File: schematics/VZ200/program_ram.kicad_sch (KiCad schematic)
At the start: 4 parts, among them U101 74LS138, U102 6116, U103 6116, U104 6116

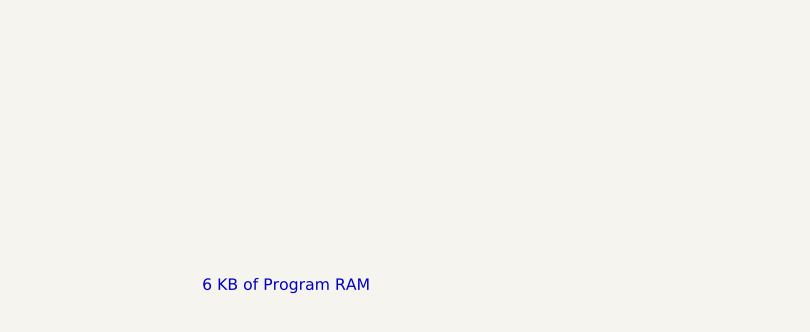
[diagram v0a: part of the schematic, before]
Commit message: Schematic for the VZ200 printer interface
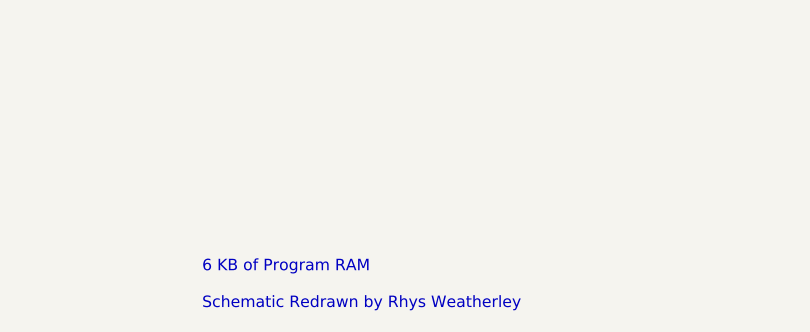
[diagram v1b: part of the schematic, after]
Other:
- note added: "6 KB of Program RAM Schematic Redrawn by Rhys Weatherley"
- note removed: "6 KB of Program RAM"
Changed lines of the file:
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@@
     (effects (font (size 1.27 1.27)) (justify left bottom))
   )
-  (text "6 KB of Program RAM" (at 184.785 174.625 0)
+  (text "6 KB of Program RAM\n\nSchematic Redrawn by Rhys Weatherley"
+    (at 184.785 176.53 0)
     (effects (font (size 1.27 1.27)) (justify left bottom))
   )

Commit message: Mention that the 6K of Program RAM is on a separate PCB
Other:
- note added: "Program RAM Schematic Redrawn by Rhys Weatherley"
- note added: "The original schematic listed these chips as U1' - U4' They have been renumbered to U101 - U104 here. The 6K of Program RAM is on a separate PCB for the VZ200. The Laser 210 only had 2K of Program RAM, which corresponds to U102 in this schematic. U101, U103, and U104 are not present on the Laser 210."
- note removed: "6 KB of Program RAM Schematic Redrawn by Rhys Weatherley"
- note removed: "The original schematic listed these chips as U1' - U4' They have been renumbered to U101 - U104 here."
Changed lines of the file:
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@@
     (stroke (width 0) (type default))
   )
-  (text "The original schematic listed these chips as U1' - U4'\nThey have been renumbered to U101 - U104 here."
-    (at 142.875 135.255 0)
+  (text "The original schematic listed these chips as U1' - U4'\nThey have been renumbered to U101 - U104 here.  The 6K of\nProgram RAM is on a separate PCB for the VZ200.\n\nThe Laser 210 only had 2K of Program RAM, which corresponds\nto U102 in this schematic.  U101, U103, and U104 are not\npresent on the Laser 210."
+    (at 135.89 144.78 0)
     (effects (font (size 1.27 1.27)) (justify left bottom))
   )
@@
     (effects (font (size 1.27 1.27)) (justify left bottom))
   )
-  (text "6 KB of Program RAM\n\nSchematic Redrawn by Rhys Weatherley"
-    (at 184.785 176.53 0)
+  (text "Program RAM\n\nSchematic Redrawn by Rhys Weatherley" (at 184.785 176.53 0)
     (effects (font (size 1.27 1.27)) (justify left bottom))
   )

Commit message: Add title and revision details to the schematic sheets
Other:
- title: (none) -> VZ200 Computer
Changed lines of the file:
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@@
 (kicad_sch (version 20230121) (generator eeschema)
   (paper "A4")
+  (title_block
+    (title "VZ200 Computer")
+    (date "2024-01-01")
+    (rev "1")
+  )
   (junction (at 130.175 44.45) (diameter 0) (color 0 0 0 0)
   )

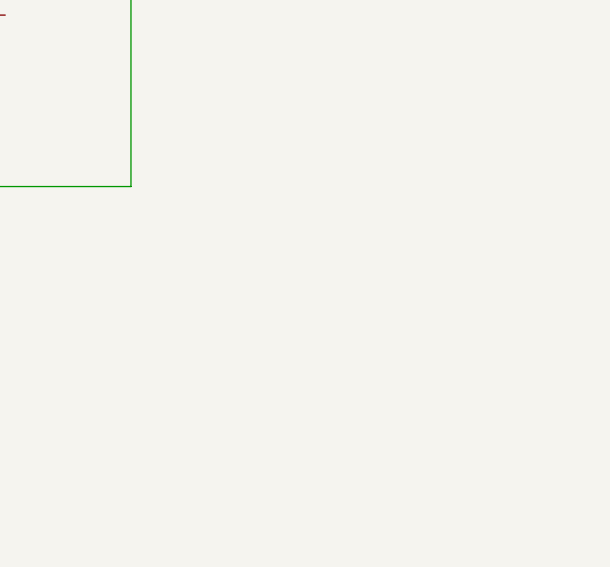
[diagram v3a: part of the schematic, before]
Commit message: Update motherboard schematic based on inspection of the actual board
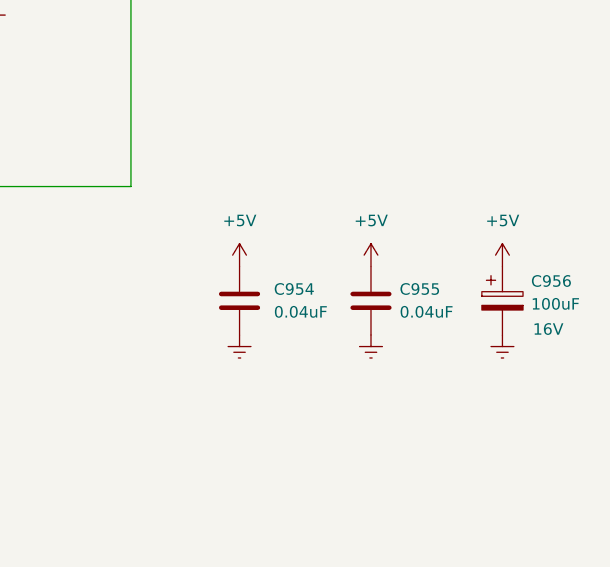
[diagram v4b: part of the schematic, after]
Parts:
- added C954, C955: 0.04uF, symbol Device:C
- added C956: 100uF, symbol Device:C_Polarized
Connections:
- net +5V: now also C954.1, C955.1, C956.1
- net Earth: now also C954.2, C955.2, C956.2
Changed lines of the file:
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@@
   (title_block
     (title "VZ200 Computer")
-    (date "2024-01-01")
-    (rev "1")
+    (date "2024-01-05")
+    (rev "2")
   )
   (junction (at 130.175 44.45) (diameter 0) (color 0 0 0 0)
@@
     (property "Intersheetrefs" "${INTERSHEET_REFS}" (at 223.3302 96.52 0)
       (effects (font (size 1.27 1.27)) (justify left) hide)
+    )
+  )
+  (symbol (lib_id "power:+5V") (at 245.745 133.35 0) (unit 1)
+    (in_bom yes) (on_board yes) (dnp no) (fields_autoplaced)
+    (property "Reference" "#PWR0149" (at 245.745 137.16 0)
+      (effects (font (size 1.27 1.27)) hide)
+    )
+    (property "Value" "+5V" (at 245.745 128.27 0)
+      (effects (font (size 1.27 1.27)))
+    )
+    (property "Footprint" "" (at 245.745 133.35 0)
+      (effects (font (size 1.27 1.27)) hide)
+    )
+    (property "Datasheet" "" (at 245.745 133.35 0)
+      (effects (font (size 1.27 1.27)) hide)
+    )
+    (pin "1")
+    (instances
+      (project "VZ200"
+        (path "/5e5f5998-714c-4695-b6b0-5b20d6c62fd6/0f5ef76c-8fbc-47f1-bc85-d4b3dcf632f6"
+          (reference "#PWR0149") (unit 1)
+        )
+      )
+    )
+  )
+  (symbol (lib_id "power:+5V") (at 260.35 133.35 0) (unit 1)
+    (in_bom yes) (on_board yes) (dnp no) (fields_autoplaced)
+    (property "Reference" "#PWR0151" (at 260.35 137.16 0)
+      (effects (font (size 1.27 1.27)) hide)
+    )
+    (property "Value" "+5V" (at 260.35 128.27 0)
+      (effects (font (size 1.27 1.27)))
+    )
+    (property "Footprint" "" (at 260.35 133.35 0)
+      (effects (font (size 1.27 1.27)) hide)
+    )
+    (property "Datasheet" "" (at 260.35 133.35 0)
+      (effects (font (size 1.27 1.27)) hide)
+    )
+    (pin "1")
+    (instances
+      (project "VZ200"
+        (path "/5e5f5998-714c-4695-b6b0-5b20d6c62fd6/0f5ef76c-8fbc-47f1-bc85-d4b3dcf632f6"
+          (reference "#PWR0151") (unit 1)
+        )
+      )
+    )
+  )
+  (symbol (lib_id "power:Earth") (at 245.745 140.97 0) (unit 1)
+    (in_bom yes) (on_board yes) (dnp no) (fields_autoplaced)
+    (property "Reference" "#PWR0150" (at 245.745 147.32 0)
+      (effects (font (size 1.27 1.27)) hide)
+    )
+    (property "Value" "Earth" (at 245.745 144.78 0)
+      (effects (font (size 1.27 1.27)) hide)
+    )
+    (property "Footprint" "" (at 245.745 140.97 0)
+      (effects (font (size 1.27 1.27)) hide)
+    )
+    (property "Datasheet" "~" (at 245.745 140.97 0)
+      (effects (font (size 1.27 1.27)) hide)
+    )
+    (pin "1")
+    (instances
+      (project "VZ200"
+        (path "/5e5f5998-714c-4695-b6b0-5b20d6c62fd6/0f5ef76c-8fbc-47f1-bc85-d4b3dcf632f6"
+          (reference "#PWR0150") (unit 1)
+        )
+      )
     )
   )
@@
     )
   )
+  (symbol (lib_id "Device:C") (at 231.14 137.16 0) (unit 1)
+    (in_bom yes) (on_board yes) (dnp no) (fields_autoplaced)
+    (property "Reference" "C954" (at 234.95 135.89 0)
+      (effects (font (size 1.27 1.27)) (justify left))
+    )
+    (property "Value" "0.04uF" (at 234.95 138.43 0)
+      (effects (font (size 1.27 1.27)) (justify left))
+    )
+    (property "Footprint" "" (at 232.1052 140.97 0)
+      (effects (font (size 1.27 1.27)) hide)
+    )
+    (property "Datasheet" "~" (at 231.14 137.16 0)
+      (effects (font (size 1.27 1.27)) hide)
+    )
+    (pin "2")
+    (pin "1")
+    (instances
+      (project "VZ200"
+        (path "/5e5f5998-714c-4695-b6b0-5b20d6c62fd6/0f5ef76c-8fbc-47f1-bc85-d4b3dcf632f6"
+          (reference "C954") (unit 1)
+        )
+      )
+    )
+  )
+  (symbol (lib_id "power:Earth") (at 231.14 140.97 0) (unit 1)
+    (in_bom yes) (on_board yes) (dnp no) (fields_autoplaced)
+    (property "Reference" "#PWR0148" (at 231.14 147.32 0)
+      (effects (font (size 1.27 1.27)) hide)
+    )
+    (property "Value" "Earth" (at 231.14 144.78 0)
+      (effects (font (size 1.27 1.27)) hide)
+    )
+    (property "Footprint" "" (at 231.14 140.97 0)
+      (effects (font (size 1.27 1.27)) hide)
+    )
+    (property "Datasheet" "~" (at 231.14 140.97 0)
+      (effects (font (size 1.27 1.27)) hide)
+    )
+    (pin "1")
+    (instances
+      (project "VZ200"
+        (path "/5e5f5998-714c-4695-b6b0-5b20d6c62fd6/0f5ef76c-8fbc-47f1-bc85-d4b3dcf632f6"
+          (reference "#PWR0148") (unit 1)
+        )
+      )
+    )
+  )
+  (symbol (lib_id "power:+5V") (at 231.14 133.35 0) (unit 1)
+    (in_bom yes) (on_board yes) (dnp no) (fields_autoplaced)
+    (property "Reference" "#PWR017" (at 231.14 137.16 0)
+      (effects (font (size 1.27 1.27)) hide)
+    )
+    (property "Value" "+5V" (at 231.14 128.27 0)
+      (effects (font (size 1.27 1.27)))
+    )
+    (property "Footprint" "" (at 231.14 133.35 0)
+      (effects (font (size 1.27 1.27)) hide)
+    )
+    (property "Datasheet" "" (at 231.14 133.35 0)
+      (effects (font (size 1.27 1.27)) hide)
+    )
+    (pin "1")
+    (instances
+      (project "VZ200"
+        (path "/5e5f5998-714c-4695-b6b0-5b20d6c62fd6/0f5ef76c-8fbc-47f1-bc85-d4b3dcf632f6"
+          (reference "#PWR017") (unit 1)
+        )
+      )
+    )
+  )
   (symbol (lib_id "power:+5V") (at 99.695 64.77 0) (unit 1)
     (in_bom yes) (on_board yes) (dnp no) (fields_autoplaced)
@@
         (path "/5e5f5998-714c-4695-b6b0-5b20d6c62fd6/0f5ef76c-8fbc-47f1-bc85-d4b3dcf632f6"
           (reference "#PWR049") (unit 1)
+        )
+      )
+    )
+  )
+  (symbol (lib_id "Device:C_Polarized") (at 260.35 137.16 0) (unit 1)
+    (in_bom yes) (on_board yes) (dnp no)
+    (property "Reference" "C956" (at 263.525 135.001 0)
+      (effects (font (size 1.27 1.27)) (justify left))
+    )
+    (property "Value" "100uF" (at 263.525 137.541 0)
+      (effects (font (size 1.27 1.27)) (justify left))
+    )
+    (property "Footprint" "" (at 261.3152 140.97 0)
+      (effects (font (size 1.27 1.27)) hide)
+    )
+    (property "Datasheet" "~" (at 260.35 137.16 0)
+      (effects (font (size 1.27 1.27)) hide)
+    )
+    (property "Rating" "16V" (at 265.43 140.335 0)
+      (effects (font (size 1.27 1.27)))
+    )
+    (pin "2")
+    (pin "1")
+    (instances
+      (project "VZ200"
+        (path "/5e5f5998-714c-4695-b6b0-5b20d6c62fd6/0f5ef76c-8fbc-47f1-bc85-d4b3dcf632f6"
+          (reference "C956") (unit 1)
+        )
+      )
+    )
+  )
+  (symbol (lib_id "Device:C") (at 245.745 137.16 0) (unit 1)
+    (in_bom yes) (on_board yes) (dnp no) (fields_autoplaced)
+    (property "Reference" "C955" (at 248.92 135.89 0)
+      (effects (font (size 1.27 1.27)) (justify left))
+    )
+    (property "Value" "0.04uF" (at 248.92 138.43 0)
+      (effects (font (size 1.27 1.27)) (justify left))
+    )
+    (property "Footprint" "" (at 246.7102 140.97 0)
+      (effects (font (size 1.27 1.27)) hide)
+    )
+    (property "Datasheet" "~" (at 245.745 137.16 0)
+      (effects (font (size 1.27 1.27)) hide)
+    )
+    (pin "2")
+    (pin "1")
+    (instances
+      (project "VZ200"
+        (path "/5e5f5998-714c-4695-b6b0-5b20d6c62fd6/0f5ef76c-8fbc-47f1-bc85-d4b3dcf632f6"
+          (reference "C955") (unit 1)
         )
       )
@@
         )
       )
+    )
+  )
+  (symbol (lib_id "power:Earth") (at 260.35 140.97 0) (unit 1)
+    (in_bom yes) (on_board yes) (dnp no) (fields_autoplaced)
+    (property "Reference" "#PWR0152" (at 260.35 147.32 0)
+      (effects (font (size 1.27 1.27)) hide)
+    )
+    (property "Value" "Earth" (at 260.35 144.78 0)
+      (effects (font (size 1.27 1.27)) hide)
+    )
+    (property "Footprint" "" (at 260.35 140.97 0)
+      (effects (font (size 1.27 1.27)) hide)
+    )
+    (property "Datasheet" "~" (at 260.35 140.97 0)
+      (effects (font (size 1.27 1.27)) hide)
+    )
+    (pin "1")
+    (instances
+      (project "VZ200"
+        (path "/5e5f5998-714c-4695-b6b0-5b20d6c62fd6/0f5ef76c-8fbc-47f1-bc85-d4b3dcf632f6"
+          (reference "#PWR0152") (unit 1)
+        )
+      )
